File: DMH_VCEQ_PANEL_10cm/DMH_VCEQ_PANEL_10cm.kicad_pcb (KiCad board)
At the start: 2 copper layers, 100 x 200 mm, 35 parts

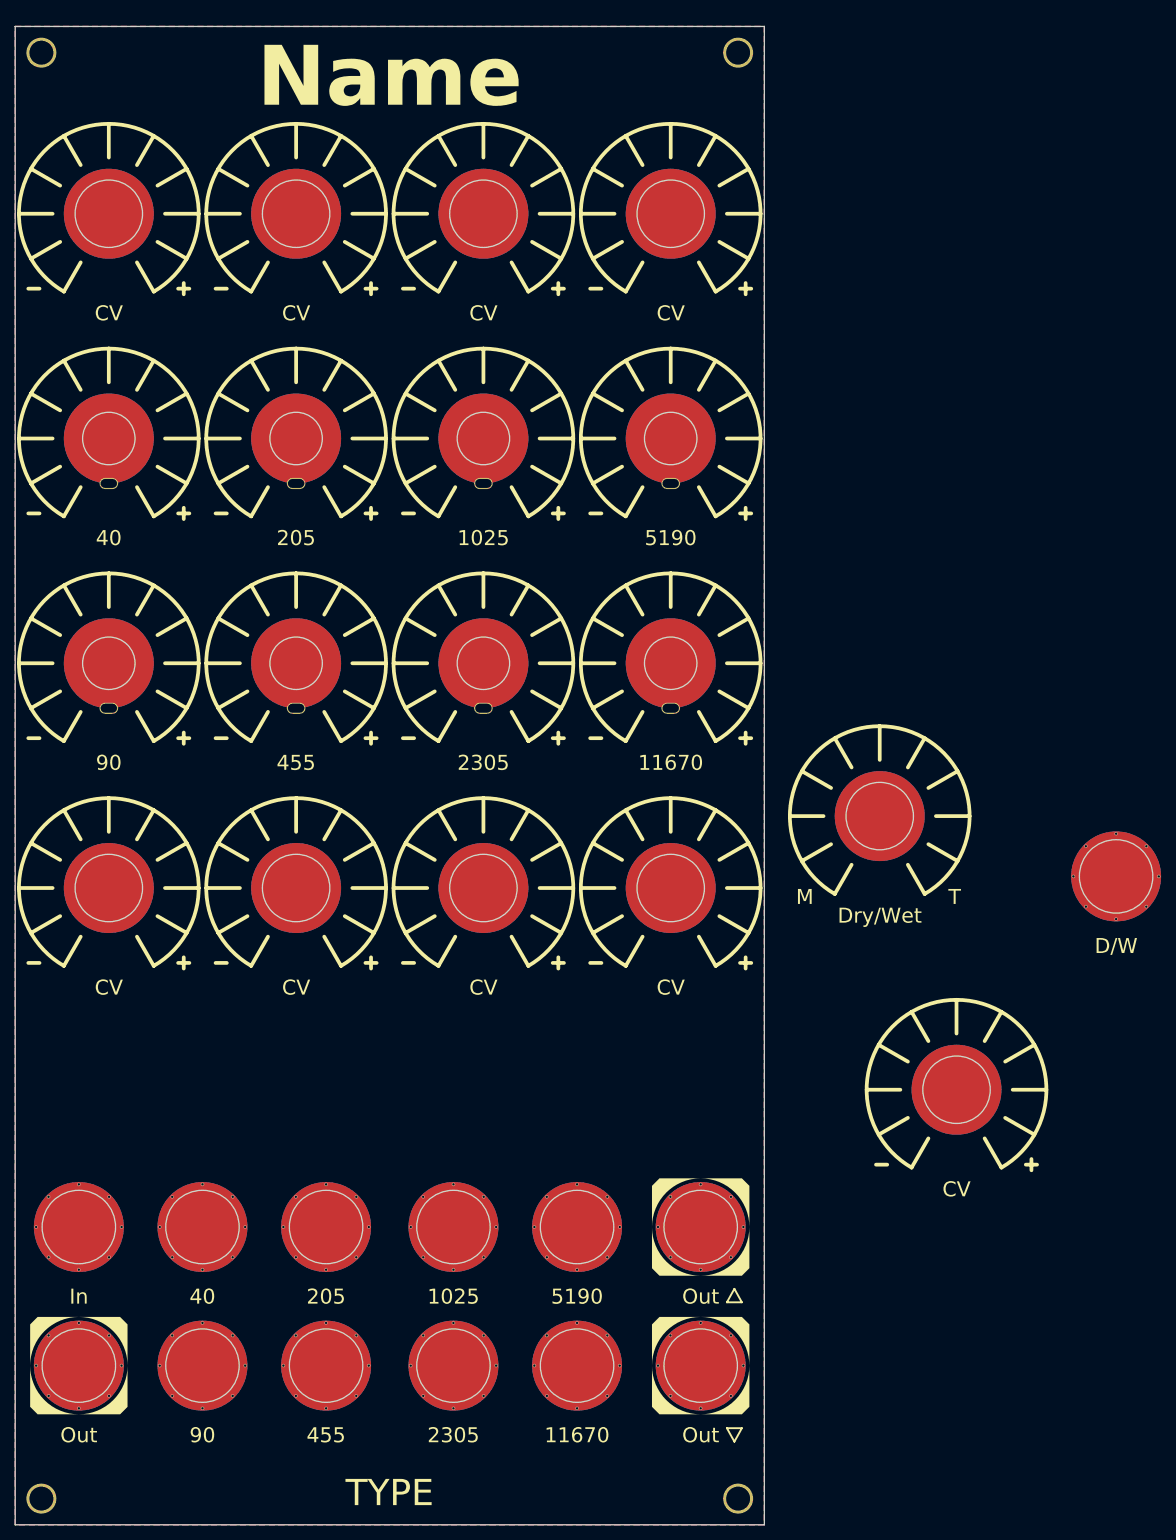
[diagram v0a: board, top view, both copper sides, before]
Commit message: Designed 10cm panel
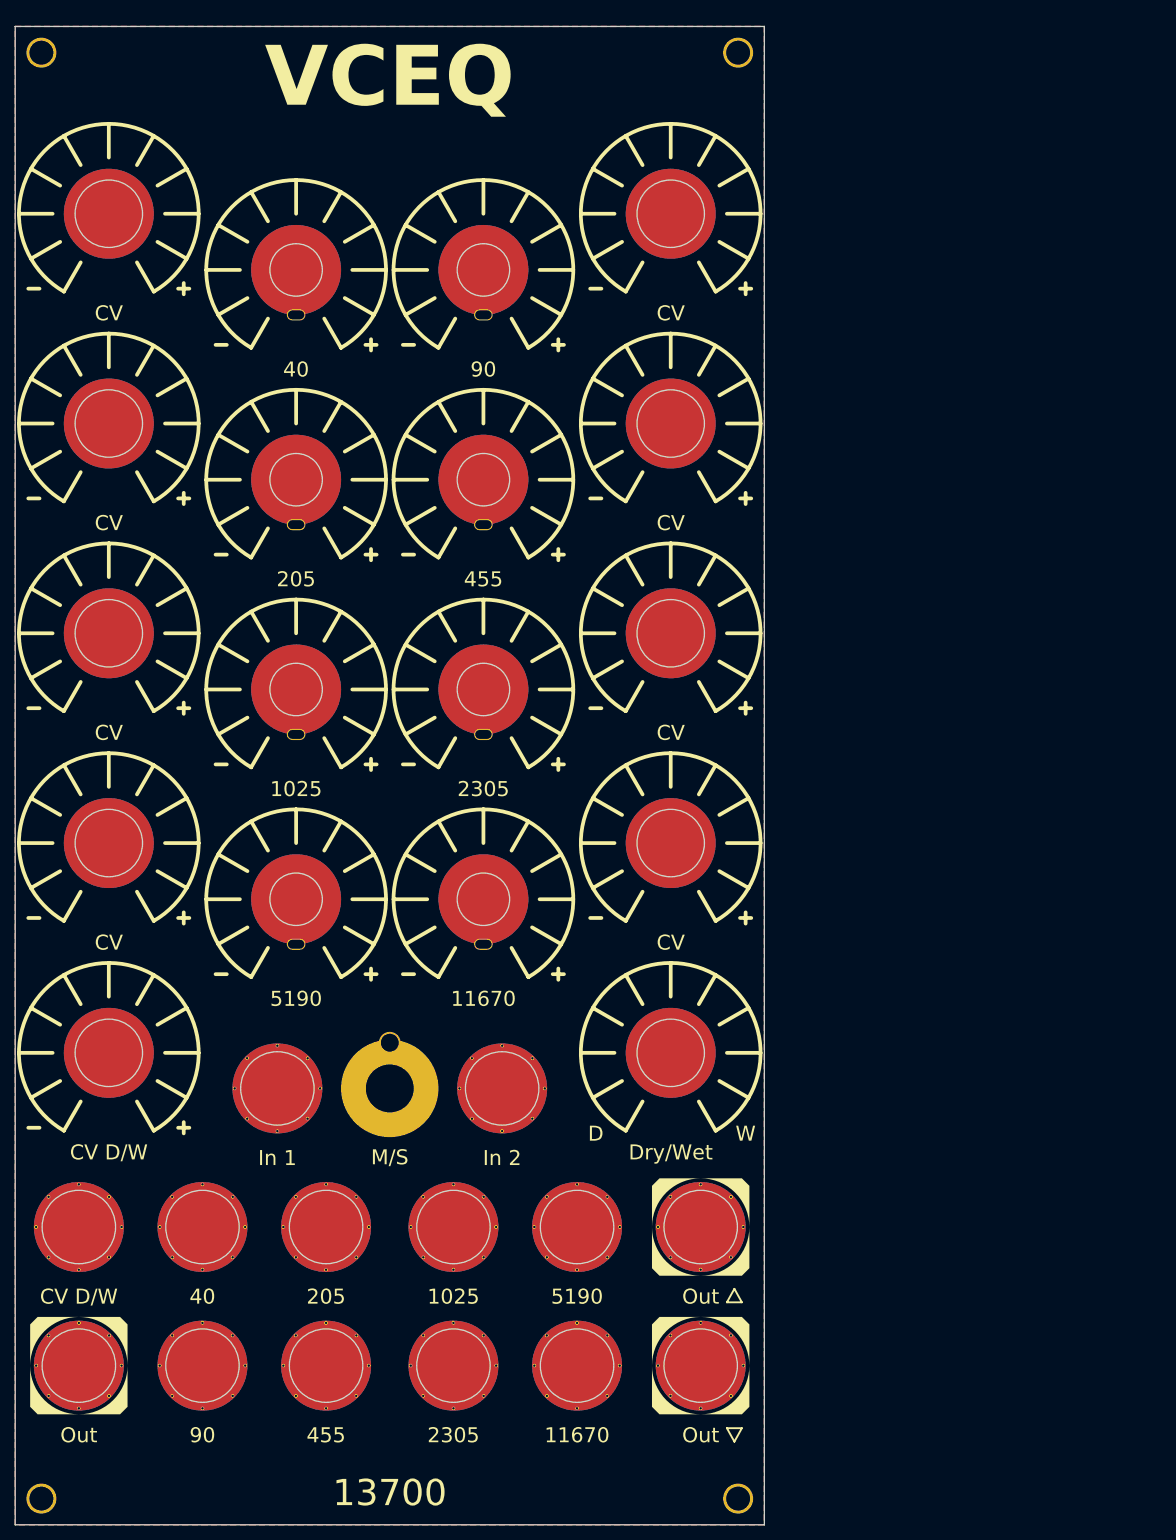
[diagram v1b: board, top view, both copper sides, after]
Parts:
- added H36: In 2, SynthStuff:Jack_6.35mm_Cutout_v3, F.Cu at (115.0, 171.8)
- added H37: M/S, SynthStuff:Toggle_Switch_TE_Cutout, F.Cu at (100.0, 171.8)
- H21: value In -> In 1
- H22, H23: value Out -> Out
- H33: value D/W -> CV D/W
- H35: value CV -> CV D/W
- moved H33 146.1 mm to (58.5, 190.2)
- moved H35 113.3 mm to (62.5, 167.0)
- moved H28 79.6 mm to (137.5, 83.0)
- moved H11 79.3 mm to (87.5, 146.5)
- moved H29 75.1 mm to (62.5, 111.0)
- moved H6 72.5 mm to (112.5, 62.5)
- moved H30 42.2 mm to (137.5, 111.0)
- moved H34 42.2 mm to (137.5, 167.0)
- moved H9 41.8 mm to (87.5, 118.5)
- moved H12 40.2 mm to (112.5, 146.5)
- moved H27 37.5 mm to (62.5, 83.0)
- moved H8 35.0 mm to (112.5, 90.5)
- moved H5 33.6 mm to (87.5, 62.5)
- moved H21 32.3 mm to (85.0, 171.8)
- moved H26 6.00 mm to (62.5, 139.0)
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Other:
- board text added: "13700"
- board text added: "VCEQ"
- board text removed: "Name"
- board text removed: "TYPE"

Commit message: Improving 10cm version
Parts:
- removed H37: M/S, SynthStuff:Toggle_Switch_TE_Cutout
- added H39: FB, SynthStuff:Jack_6.35mm_Cutout_v3, F.Cu at (100.0, 171.8)
- H22: value Out -> Dry/Wet; footprint SynthStuff:Jack_6.35mm_Cutout_Output_v6 -> SynthStuff:Jack_6.35mm_Cutout_v3
- H23, H24: value Out -> Out
- H33: value CV D/W -> Out; footprint SynthStuff:Jack_6.35mm_Cutout_v3 -> SynthStuff:Jack_6.35mm_Cutout_Output_v6
- H34: value Dry/Wet -> In 2 [FB]; footprint SynthStuff:Pot_Cutout_Tiny_text_P110KH1 -> SynthStuff:Pot_Cutout_Tiny
- H35: value CV D/W -> In 1; footprint SynthStuff:Pot_Cutout_Tiny_attv_P110KH1 -> SynthStuff:Pot_Cutout_Tiny
- moved H22 18.5 mm to (141.5, 190.2)
- moved H23 18.5 mm to (141.5, 208.8)
- moved H21 1.50 mm to (83.5, 171.8)
- moved H36 1.50 mm to (116.5, 171.8)

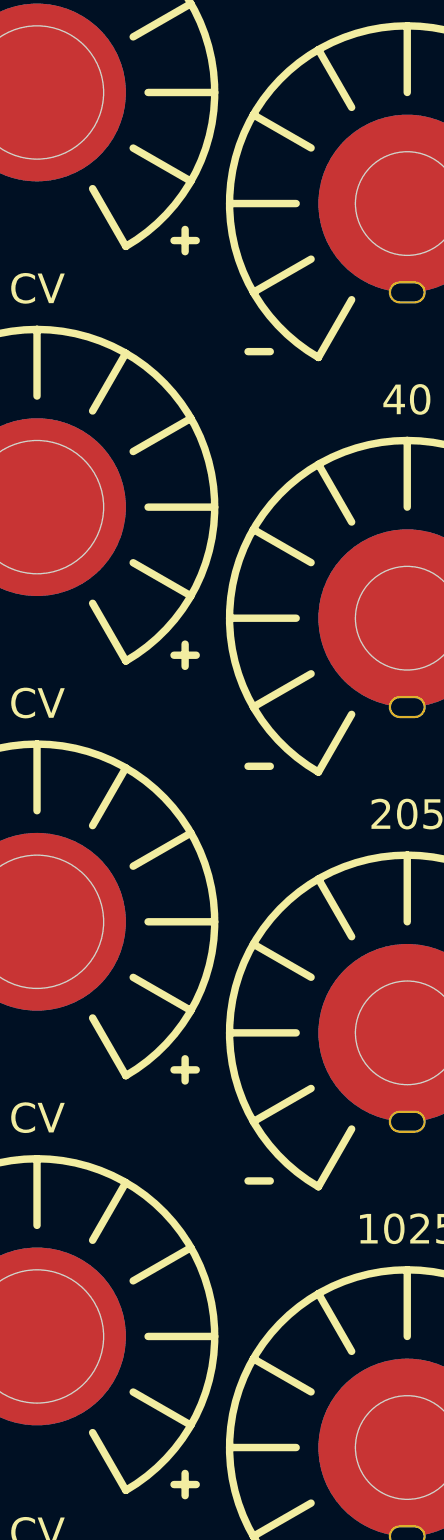
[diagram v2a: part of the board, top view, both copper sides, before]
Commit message: Finished 15 and 10 panels
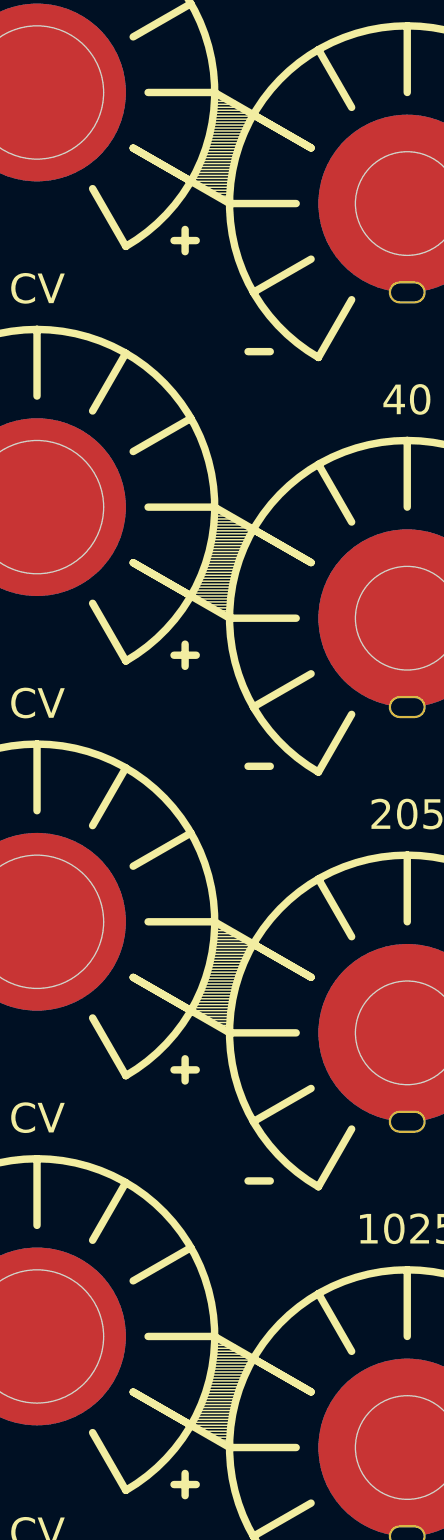
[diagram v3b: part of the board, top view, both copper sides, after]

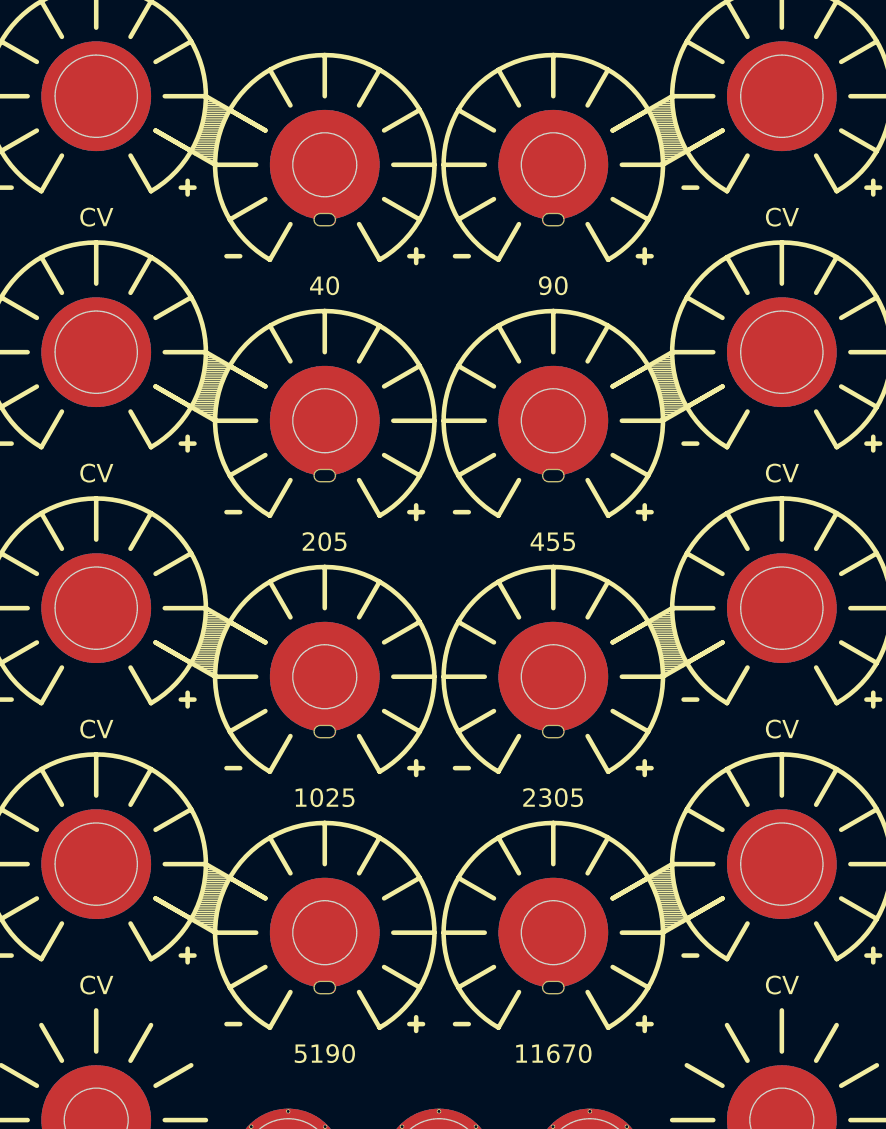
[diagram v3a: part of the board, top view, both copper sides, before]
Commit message: Pushed CV knobs inwards
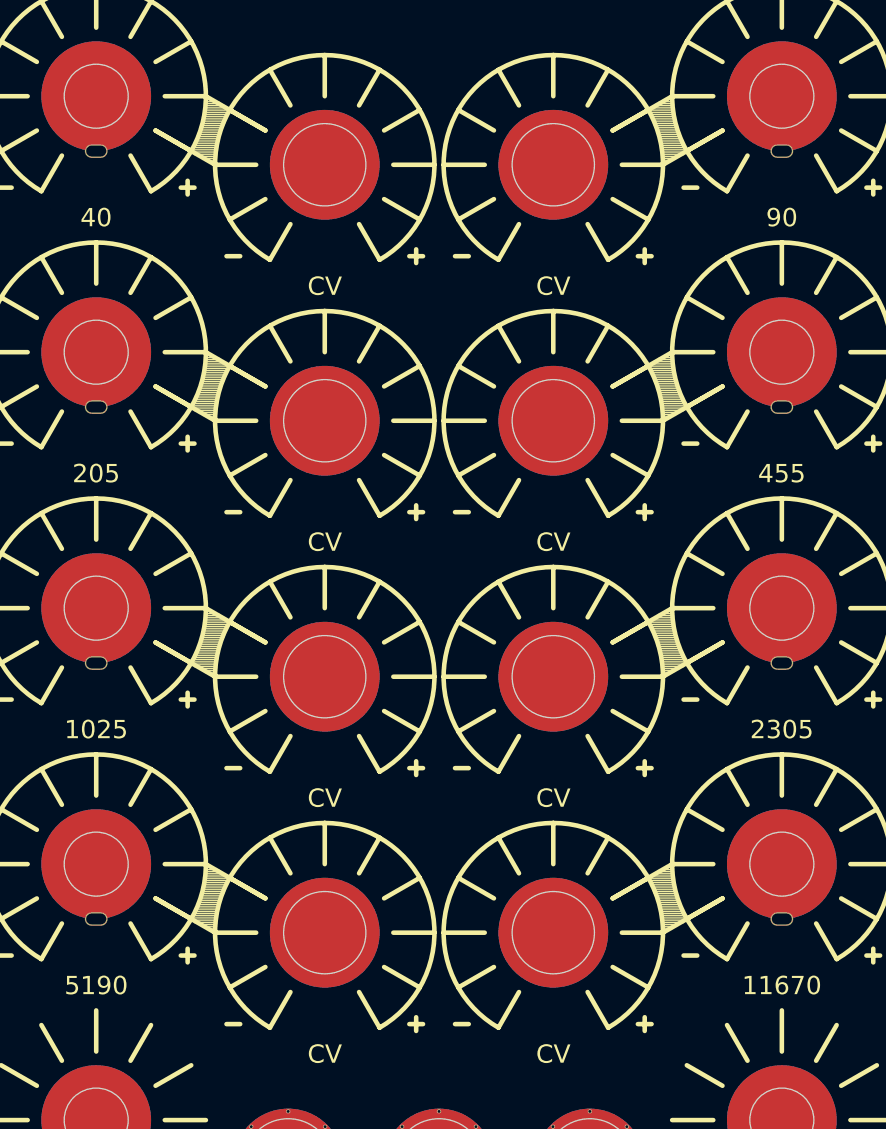
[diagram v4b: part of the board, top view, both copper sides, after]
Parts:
- moved H10 26.1 mm to (137.5, 111.0)
- moved H11 26.1 mm to (62.5, 139.0)
- moved H12 26.1 mm to (137.5, 139.0)
- moved H25 26.1 mm to (87.5, 62.5)
- moved H26 26.1 mm to (87.5, 146.5)
- moved H27 26.1 mm to (87.5, 90.5)
- moved H28 26.1 mm to (112.5, 90.5)
- moved H29 26.1 mm to (87.5, 118.5)
- moved H30 26.1 mm to (112.5, 118.5)
- moved H31 26.1 mm to (112.5, 62.5)
- moved H32 26.1 mm to (112.5, 146.5)
- moved H5 26.1 mm to (62.5, 55.0)
- moved H6 26.1 mm to (137.5, 55.0)
- moved H7 26.1 mm to (62.5, 83.0)
- moved H8 26.1 mm to (137.5, 83.0)
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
